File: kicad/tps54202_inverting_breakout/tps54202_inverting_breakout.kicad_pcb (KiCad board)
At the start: 2 copper layers, 33 x 37.3 mm, 23 parts, among them J1 Conn_01x04, J3 ENABLE, U1 TPS54202DDC

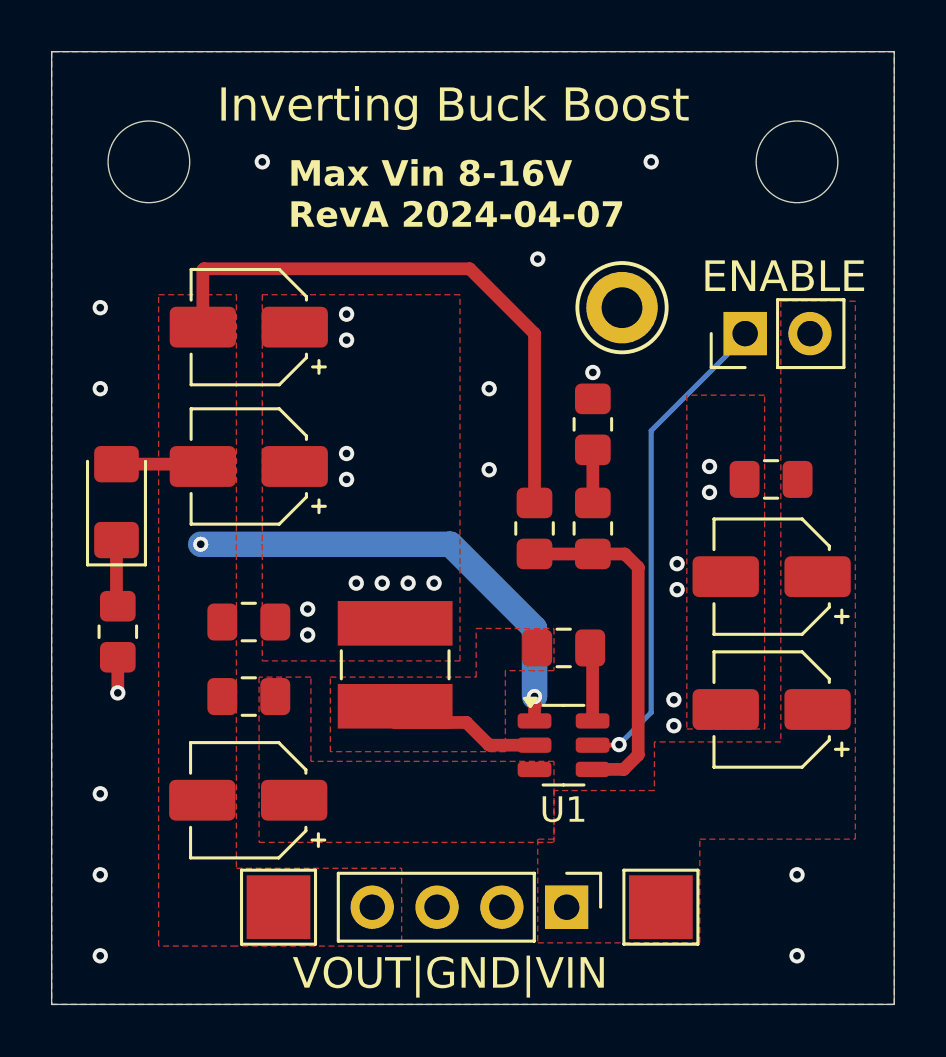
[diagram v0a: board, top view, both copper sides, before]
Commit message: RevB layout, added outut caps, tighter bypass coupling, improved layout
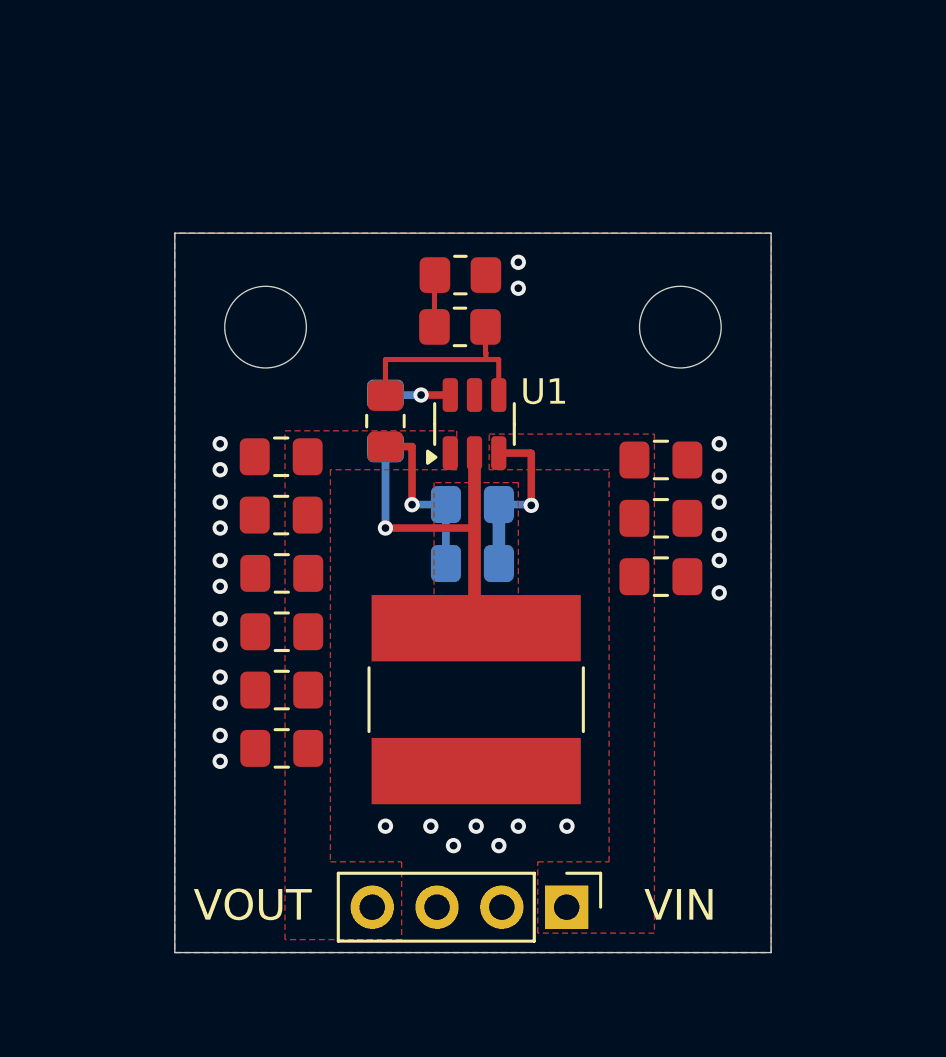
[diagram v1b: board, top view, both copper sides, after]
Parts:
- removed D1: LED, LED_SMD:LED_1206_3216Metric_Pad1.42x1.75mm_HandSolder
- removed J3: ENABLE, Connector_PinHeader_2.54mm:PinHeader_1x02_P2.54mm_Vertical
- removed R4: 2K7, Resistor_SMD:R_0805_2012Metric_Pad1.20x1.40mm_HandSolder
- removed TP1, TP2: TestPoint, TestPoint:TestPoint_Pad_2.5x2.5mm
- removed TP3: TestPoint, TestPoint:TestPoint_Keystone_5005-5009_Compact
- added C10: 22uF, Capacitor_SMD:C_0805_2012Metric_Pad1.18x1.45mm_HandSolder, F.Cu at (189.4, 95.2)
- added C11: 22uF, Capacitor_SMD:C_0805_2012Metric_Pad1.18x1.45mm_HandSolder, F.Cu at (189.4, 97.5)
- added C12: 22uF, Capacitor_SMD:C_0805_2012Metric_Pad1.18x1.45mm_HandSolder, F.Cu at (189.4, 99.8)
- C2, C3, C4, C5: footprint Capacitor_SMD:CP_Elec_4x3 -> Capacitor_SMD:C_0805_2012Metric_Pad1.18x1.45mm_HandSolder
- C7: footprint Capacitor_SMD:CP_Elec_4x3 -> Capacitor_SMD:C_0805_2012Metric_Pad1.18x1.45mm_HandSolder; moved to B.Cu
- C8, C9: moved to B.Cu
- L1: footprint Inductor_SMD:L_Ferrocore_DLG-0403 -> Inductor_SMD:L_Bourns-SRN8040_8x8.15mm
- moved C7 14.5 mm to (196.8, 90.3)
- moved U1 13.1 mm to (196.9, 87.1), turned to 90 degrees
- moved C9 11.3 mm to (193.4, 87.0), turned to -90 degrees
- moved C4 10.7 mm to (204.2, 88.5), turned to 0 degrees
- moved C8 10.2 mm to (196.8, 92.6)
- moved R2 9.46 mm to (196.3, 83.3), turned to 180 degrees
- moved H1 7.93 mm to (188.7, 83.3)
- moved H2 7.93 mm to (205.0, 83.3)
- moved R1 7.82 mm to (196.4, 81.3), turned to 0 degrees
- moved C2 7.47 mm to (189.3, 90.7), turned to 0 degrees
- moved R3 7.20 mm to (193.4, 87.0), turned to 90 degrees
- moved C1 6.60 mm to (189.3, 88.4), turned to 0 degrees
- moved C6 5.76 mm to (204.2, 93.1), turned to 0 degrees
- moved C5 4.91 mm to (204.2, 90.8), turned to 0 degrees
- moved C3 4.39 mm to (189.4, 93.0), turned to 0 degrees
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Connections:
- U1 pad 5: Net-(J3-Pin_1) -> unconnected-(U1-EN-Pad5)
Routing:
- net /VOUT: track 44.4 -> 6.96 mm, vias 2 -> 1
- net Net-(J3-Pin_1): track 19.2 -> 0.00 mm, vias 1 -> 0
- net Net-(U1-SW): track 5.86 -> 17.5 mm, vias 0 -> 1
- net /VIN: track 0.17 -> 6.88 mm, vias 0 -> 1
- net /VSENSE: track 13.7 -> 8.56 mm
- net Net-(D1-K): track 2.52 -> 0.00 mm
- net GND: track 1.42 -> 0.00 mm, vias 30 -> 27
- net Net-(U1-BOOT): track 2.91 -> 2.55 mm, vias 0 -> 1
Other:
- board size 33 x 37.3 mm -> 23.4 x 28.2 mm
- board text added: "VIN"
- board text added: "VOUT"
- board text removed: "ENABLE"
- board text removed: "VOUT|GND|VIN"
